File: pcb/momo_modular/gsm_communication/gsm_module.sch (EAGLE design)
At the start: 18 parts

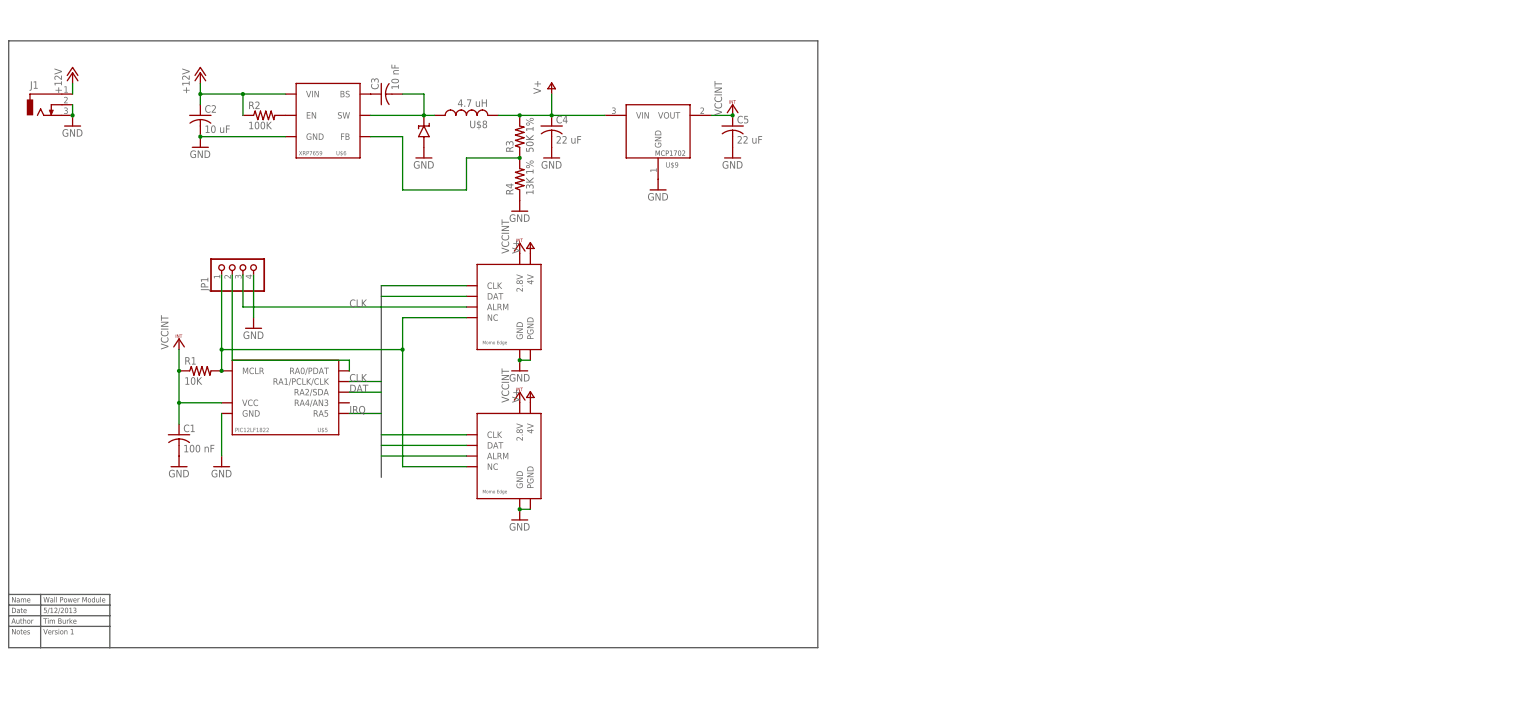
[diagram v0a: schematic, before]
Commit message: Laid out version 2 of the controller board and wall power board with better power supply layout to minimize noise coupling. Created version 1 of the gsm board. Changed Momo edge connector to an 8 pin version.
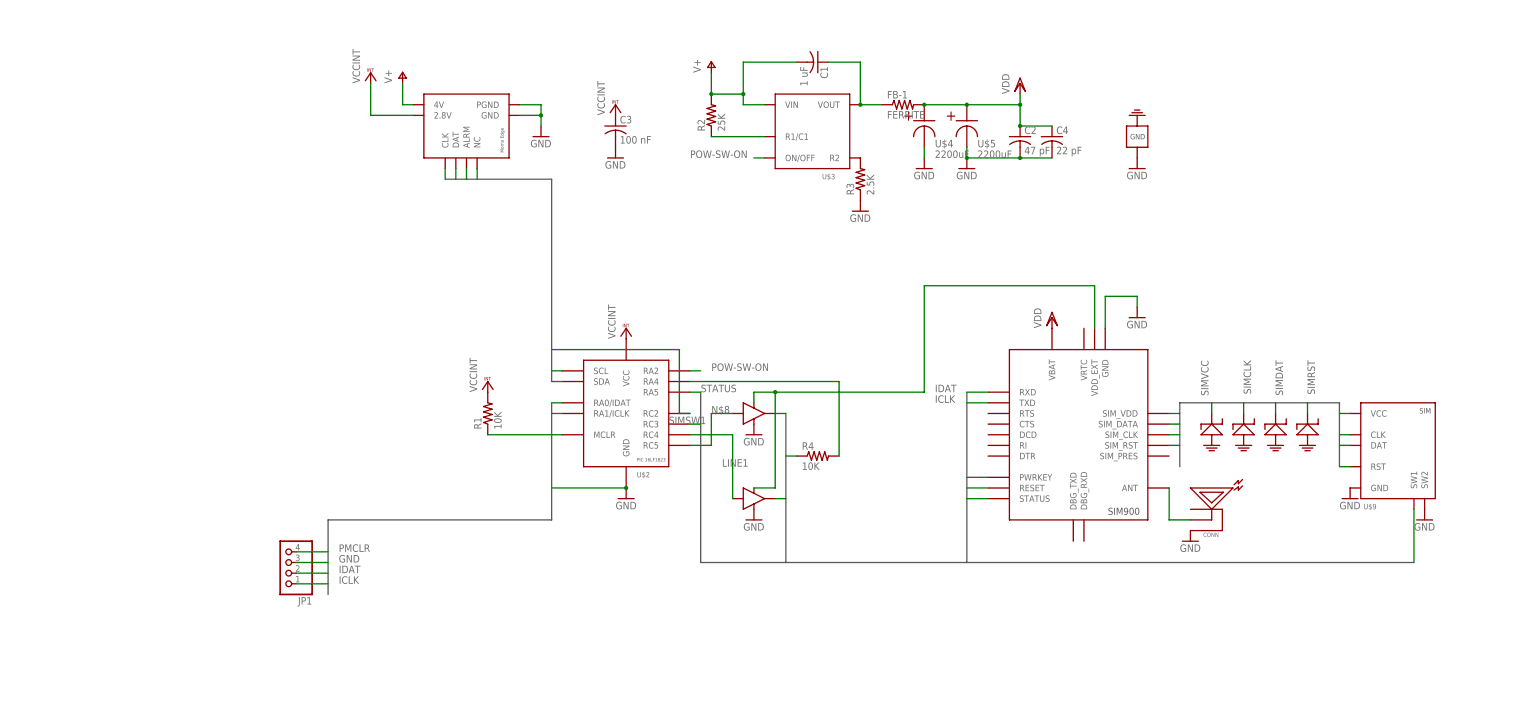
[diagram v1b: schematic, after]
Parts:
- removed C5: 22 uF, rcl:C-USC0402
- removed J1: (no value), con-jack:DCJ0303
- added CONN: RFANTENNA, components:RFANTENNA
- added FB-1: FERRITE, rcl:R-US_R0805
- added U$3: TI-HIGHSIDE-PFET, components:TI-HIGHSIDE-PFET
- added U$4: 2200uF, components:CAP-2200UF
- added U10: ESD-SMF05C, components:ESD-SMF05C
- C1: value 100 nF -> 1 uF; device rcl:C-USC0402 -> rcl:C-USC0402K
- C2: value 10 uF -> 47 pF; device rcl:C-USC0805 -> rcl:C-USC0402K
- C3: value 10 nF -> 100 nF
- C4: value 22 uF -> 22 pF; device rcl:C-USC1206 -> rcl:C-USC0402K
- R2: value 100K -> 25K
- R3: value 50K 1% -> 2.5K
- R4: value 13K 1% -> 10K
- U$1: value MOMO-EDGE-8F -> MOMO-EDGE-8M; device components:MOMO-EDGE-8F -> components:MOMO-EDGE-8M
- U$2: value MOMO-EDGE-8M -> PIC16LF1823; device components:MOMO-EDGE-8M -> components:PIC16LF1823
- U$5: value PIC12LF1822 -> 2200uF; device components:PIC12LF1822 -> components:CAP-2200UF
- U$6: value XRP7659 -> SIM900; device components:XRP7659 -> components:SIM900
- U$7: value DIODE_SS2P3 -> BUFFER-OD; device components:DIODE_SS2P3 -> components:BUFFER-OD
- U$8: value 4.7 uH -> BUFFER-OD; device components:NR6028-INDUCTOR -> components:BUFFER-OD
- U$9: value MCP1702 -> SIMHOLDER-8PIN; device components:MCP1702 -> components:SIMHOLDER-8PIN
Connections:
- removed net +12V: C2.1, J1.1, R2.1, U$6.VIN
- removed net CLK: JP1.3, U$1.CLK, U$2.CLK, U$5.RA1/PCLK/CLK
- removed net IRQ: U$1.ALRM, U$2.ALRM, U$5.RA5
- new net ALARM: U$1.ALRM, U$2.RC2
- new net CLOCK: U$1.CLK, U$2.SCL
- new net ICLK: JP1.1, U$2.RA1/ICLK, U$6.TXD
- new net IDAT: JP1.2, U$2.RA0/IDAT, U$6.RXD
- new net LINE1: U$2.RC4, U$8.IN
- new net N$7: CONN.PIN, U$6.ANT
- new net PMCLR: JP1.4, R1.1, U$1.NC, U$2.MCLR
- new net POW-SW-ON: U$2.RA2, U$3.ON/OFF
- new net PWRKEY: U$6.PWRKEY, U$7.OUT
- new net RESET: U$6.RESET, U$8.OUT
- new net SIMCLK: U$6.SIM_CLK, U$9.CLK, U10G$4.P$1
- new net SIMDAT: U$6.SIM_DATA, U$9.DAT, U10G$3.P$1
- new net SIMRST: U$6.SIM_RST, U$9.RST, U10G$2.P$1
- new net SIMSW1: R4.1, U$2.RC3, U$9.SW1
- new net SIMVCC: U$6.SIM_VDD, U$9.VCC, U10G$1.P$1
- new net STATUS: U$2.RA5, U$6.STATUS
- new net VDD: C2.1, C4.1, FB-1.2, U$4.+, U$5.+, U$6.VBAT
- net DAT: now also U$2.SDA; no longer U$2.DAT, U$5.RA2/SDA
- net GND: now also C3.2, CONN.SHIELD, JP1.3, R3.1, U$4.-, U$5.-, U$7.GND, U$8.GND, U$9.SW2, U10G$6.GND; no longer C1.2, C5.2, J1.2, J1.3, JP1.4, R4.1, U$2.PGND, U$5.GND, U$7.AN
- net N$1: now also R3.2, U$3.R2; no longer JP1.1, R1.2, U$1.NC, U$2.NC, U$5.MCLR
- net N$2: now also R4.2, U$2.RA4; no longer C3.2, U$6.SW, U$7.CATH, U$8.1
- net N$3: now also R2.1, U$3.R1/C1; no longer R2.2, U$6.EN
- net N$4: now also C1.1, FB-1.1, U$3.VOUT; no longer C3.1, U$6.BS
- net N$6: now also U$6.VDD_EXT, U$7.VCC, U$8.VCC; no longer R3.1, R4.2, U$6.FB
- net N$8: now also U$2.RC5, U$7.IN; no longer JP1.2, U$5.RA0/PDAT
- net V+: now also C1.2, R2.2, U$3.VIN; no longer C4.1, R3.2, U$2.4V, U$8.2, U$9.VIN
- net VCCINT: now also C3.1, R1.2, U$2.VCC; no longer C1.1, C5.1, R1.1, U$2.2.8V, U$5.VCC, U$9.VOUT
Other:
- note removed: "5/12/2013"
- note removed: "Author"
- note removed: "Date"
- note removed: "Name"
- note removed: "Notes"
- note removed: "Tim Burke"
- note removed: "Version 1"
- note removed: "Wall Power Module"
- moved on the sheet: C1, C2, C3, C4, JP1, R1, R2, R3, R4

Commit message: Finalized the following boards for fabrication/assembly: Sensor Dev Board GSM Module Combined Wallpower and Controller Boards
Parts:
- removed U$7, U$8: BUFFER-OD, components:BUFFER-OD
- added JP2: (no value), pinhead:PINHD-1X3
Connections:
- removed net LINE1: U$2.RC4, U$8.IN
- removed net N$6: U$6.VDD_EXT, U$7.VCC, U$8.VCC
- removed net N$8: U$2.RC5, U$7.IN
- new net DEBUGRX: JP2.2, U$6.DBG_RXD
- new net DEBUGTX: JP2.1, U$6.DBG_TXD
- net GND: now also JP2.3; no longer U$7.GND, U$8.GND
- net PWRKEY: now also U$2.RC5; no longer U$7.OUT
- net RESET: now also U$2.RC4; no longer U$8.OUT
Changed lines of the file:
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@@
 <part name="VDD2" library="supply1" deviceset="VDD" device=""/>
 <part name="GND7" library="supply1" deviceset="GND" device=""/>
-<part name="U$7" library="components" deviceset="BUFFER-OD" device=""/>
-<part name="U$8" library="components" deviceset="BUFFER-OD" device=""/>
-<part name="GND8" library="supply1" deviceset="GND" device=""/>
-<part name="GND9" library="supply1" deviceset="GND" device=""/>
 <part name="U$9" library="components" deviceset="SIMHOLDER-8PIN" device=""/>
 <part name="GND10" library="supply1" deviceset="GND" device=""/>
@@
 <part name="C4" library="rcl" deviceset="C-US" device="C0402K" value="22 pF"/>
 <part name="R4" library="rcl" deviceset="R-US_" device="R0603" value="10K"/>
+<part name="JP2" library="pinhead" deviceset="PINHD-1X3" device=""/>
+<part name="GND6" library="supply1" deviceset="GND" device=""/>
 </parts>
 <sheets>
@@
 <instance part="VDD2" gate="G$1" x="152.4" y="40.64"/>
 <instance part="GND7" gate="1" x="172.72" y="40.64"/>
-<instance part="U$7" gate="G$1" x="81.28" y="17.78"/>
-<instance part="U$8" gate="G$1" x="81.28" y="-2.54"/>
-<instance part="GND8" gate="1" x="81.28" y="12.7"/>
-<instance part="GND9" gate="1" x="81.28" y="-7.62"/>
 <instance part="U$9" gate="G$1" x="226.06" y="5.08"/>
 <instance part="GND10" gate="1" x="241.3" y="-7.62"/>
@@
 <instance part="C4" gate="G$1" x="152.4" y="83.82"/>
 <instance part="R4" gate="G$1" x="96.52" y="7.62"/>
+<instance part="JP2" gate="A" x="170.18" y="-30.48"/>
+<instance part="GND6" gate="1" x="160.02" y="-40.64"/>
 </instances>
 <busses>
@@
 </segment>
 <segment>
-<pinref part="U$7" gate="G$1" pin="GND"/>
-<pinref part="GND8" gate="1" pin="GND"/>
-</segment>
-<segment>
-<pinref part="U$8" gate="G$1" pin="GND"/>
-<pinref part="GND9" gate="1" pin="GND"/>
-</segment>
-<segment>
 <pinref part="U$9" gate="G$1" pin="SW2"/>
 <pinref part="GND10" gate="1" pin="GND"/>
@@
 <pinref part="GND12" gate="1" pin="GND"/>
 <pinref part="U10" gate="G$6" pin="GND"/>
+</segment>
+<segment>
+<pinref part="GND6" gate="1" pin="GND"/>
+<wire x1="160.02" y1="-38.1" x2="160.02" y2="-33.02" width="0.1524" layer="91"/>
+<pinref part="JP2" gate="A" pin="3"/>
+<wire x1="160.02" y1="-33.02" x2="167.64" y2="-33.02" width="0.1524" layer="91"/>
 </segment>
 </net>
@@
 <net name="PWRKEY" class="0">
 <segment>
-<pinref part="U$7" gate="G$1" pin="OUT"/>
-<wire x1="86.36" y1="17.78" x2="88.9" y2="17.78" width="0.1524" layer="91"/>
+<pinref part="U$2" gate="G$1" pin="RC5"/>
+<wire x1="66.04" y1="10.16" x2="71.12" y2="10.16" width="0.1524" layer="91"/>
+<wire x1="71.12" y1="10.16" x2="71.12" y2="17.78" width="0.1524" layer="91"/>
+<label x="71.12" y="17.78" size="1.778" layer="95"/>
+<wire x1="71.12" y1="17.78" x2="88.9" y2="17.78" width="0.1524" layer="91"/>
 </segment>
 <segment>
@@
 <net name="RESET" class="0">
 <segment>
-<pinref part="U$8" gate="G$1" pin="OUT"/>
-<wire x1="86.36" y1="-2.54" x2="88.9" y2="-2.54" width="0.1524" layer="91"/>
+<pinref part="U$2" gate="G$1" pin="RC4"/>
+<wire x1="66.04" y1="12.7" x2="76.2" y2="12.7" width="0.1524" layer="91"/>
+<wire x1="76.2" y1="12.7" x2="76.2" y2="-2.54" width="0.1524" layer="91"/>
+<wire x1="76.2" y1="-2.54" x2="88.9" y2="-2.54" width="0.1524" layer="91"/>
 </segment>
 <segment>
@@
 </segment>
 </net>
-<net name="N$8" class="0">
-<segment>
-<pinref part="U$2" gate="G$1" pin="RC5"/>
-<wire x1="66.04" y1="10.16" x2="71.12" y2="10.16" width="0.1524" layer="91"/>
-<wire x1="71.12" y1="10.16" x2="71.12" y2="17.78" width="0.1524" layer="91"/>
-<pinref part="U$7" gate="G$1" pin="IN"/>
-<wire x1="71.12" y1="17.78" x2="76.2" y2="17.78" width="0.1524" layer="91"/>
-<label x="71.12" y="17.78" size="1.778" layer="95"/>
-</segment>
-</net>
-<net name="N$6" class="0">
-<segment>
-<pinref part="U$8" gate="G$1" pin="VCC"/>
-<wire x1="81.28" y1="0" x2="86.36" y2="0" width="0.1524" layer="91"/>
-<wire x1="86.36" y1="0" x2="86.36" y2="22.86" width="0.1524" layer="91"/>
-<pinref part="U$7" gate="G$1" pin="VCC"/>
-<wire x1="86.36" y1="22.86" x2="81.28" y2="22.86" width="0.1524" layer="91"/>
-<wire x1="81.28" y1="22.86" x2="81.28" y2="20.32" width="0.1524" layer="91"/>
-<wire x1="86.36" y1="22.86" x2="121.92" y2="22.86" width="0.1524" layer="91"/>
-<wire x1="121.92" y1="22.86" x2="121.92" y2="48.26" width="0.1524" layer="91"/>
-<junction x="86.36" y="22.86"/>
-<pinref part="U$6" gate="G$1" pin="VDD_EXT"/>
-<wire x1="121.92" y1="48.26" x2="162.56" y2="48.26" width="0.1524" layer="91"/>
-<wire x1="162.56" y1="48.26" x2="162.56" y2="38.1" width="0.1524" layer="91"/>
-</segment>
-</net>
-<net name="LINE1" class="0">
-<segment>
-<pinref part="U$2" gate="G$1" pin="RC4"/>
-<wire x1="66.04" y1="12.7" x2="76.2" y2="12.7" width="0.1524" layer="91"/>
-<label x="73.66" y="5.08" size="1.778" layer="95"/>
-<pinref part="U$8" gate="G$1" pin="IN"/>
-<wire x1="76.2" y1="12.7" x2="76.2" y2="-2.54" width="0.1524" layer="91"/>
-</segment>
-</net>
 <net name="N$2" class="0">
 <segment>
@@
 </segment>
 </net>
+<net name="DEBUGRX" class="0">
+<segment>
+<pinref part="U$6" gate="G$1" pin="DBG_RXD"/>
+<wire x1="160.02" y1="-12.7" x2="160.02" y2="-30.48" width="0.1524" layer="91"/>
+<pinref part="JP2" gate="A" pin="2"/>
+<wire x1="160.02" y1="-30.48" x2="167.64" y2="-30.48" width="0.1524" layer="91"/>
+</segment>
+</net>
+<net name="DEBUGTX" class="0">
+<segment>
+<pinref part="U$6" gate="G$1" pin="DBG_TXD"/>
+<pinref part="JP2" gate="A" pin="1"/>
+<wire x1="157.48" y1="-27.94" x2="157.48" y2="-12.7" width="0.1524" layer="91"/>
+<wire x1="157.48" y1="-27.94" x2="167.64" y2="-27.94" width="0.1524" layer="91"/>
+</segment>
+</net>

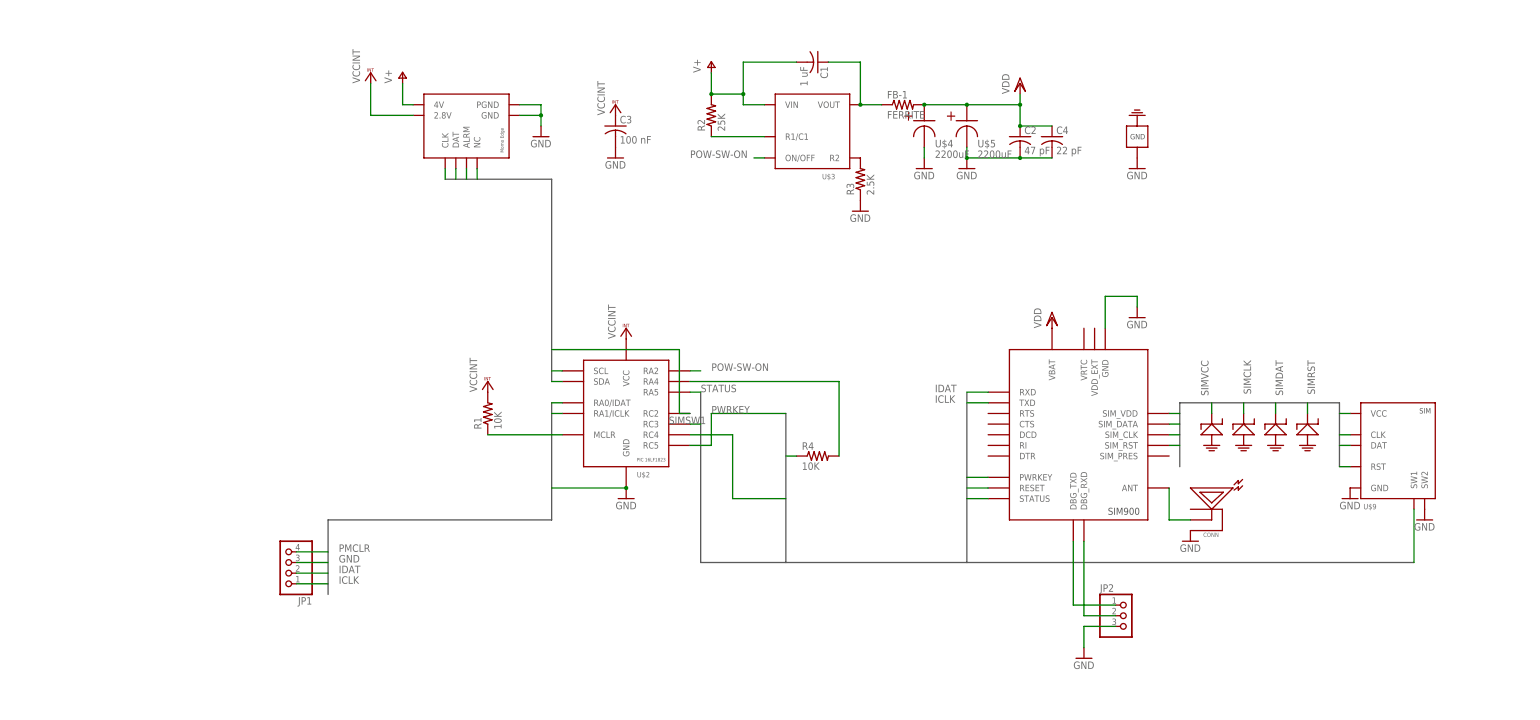
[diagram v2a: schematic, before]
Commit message: Finished next version of hardware.  Working on automatic BOM generation for purchasing.
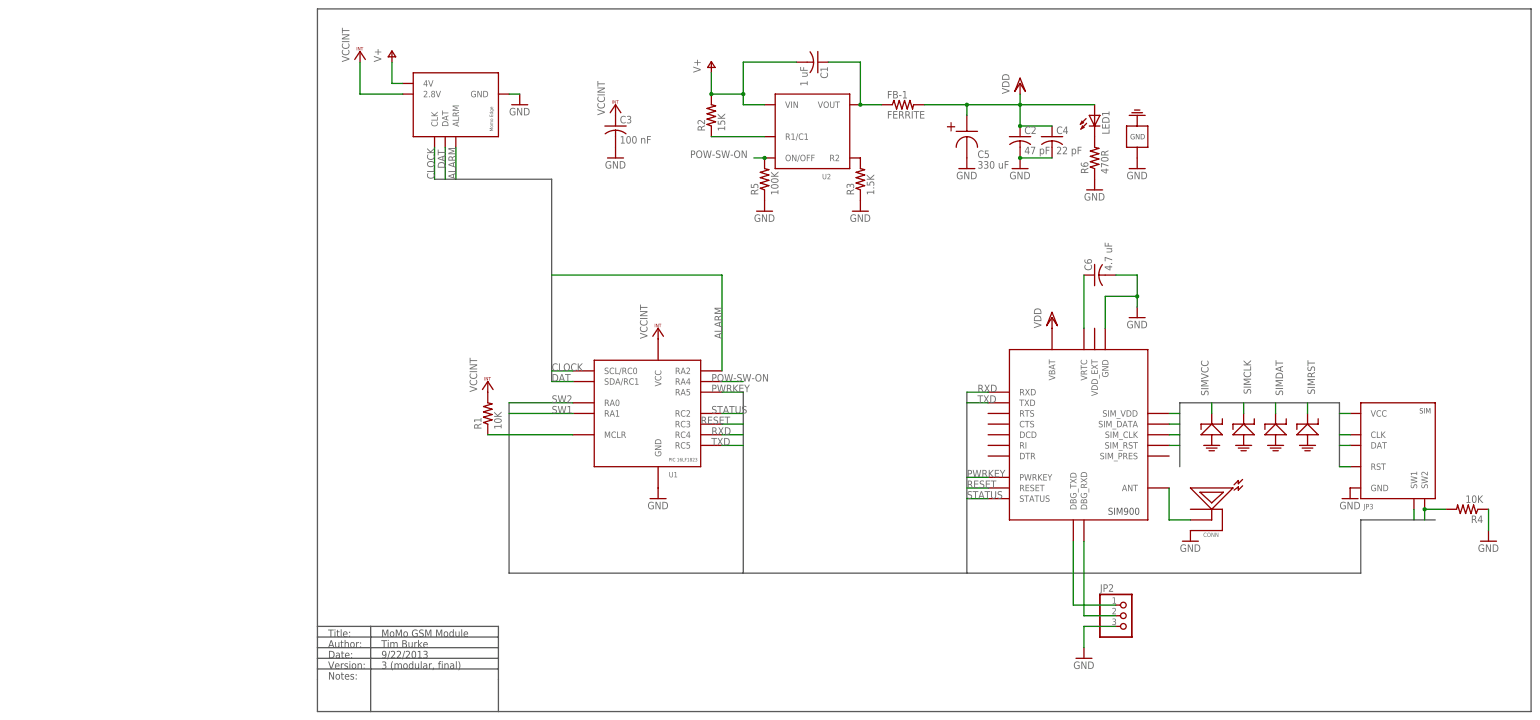
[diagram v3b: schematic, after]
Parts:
- removed U$1: MOMO-EDGE-8M, components:MOMO-EDGE-8M
- removed U$2: PIC16LF1823, components:PIC16LF1823
- removed U$4, U$5: 2200uF, components:CAP-2200UF
- removed U$9: SIMHOLDER-8PIN, components:SIMHOLDER-8PIN
- added C5: 330 uF, components:TANTALUM_CAP
- added C6: 4.7 uF, rcl:C-USC0805
- added JP3: SIMHOLDER-8PINHING, components:SIMHOLDER-8PINHING
- added LED1: (no value), led:LEDCHIPLED_0603
- added R5: 100K, rcl:R-US_R0603
- added R6: 470R, rcl:R-US_R0603
- added U1: PIC16LF1823, components:PIC16LF1823
- C1: DIGIKEY-PN (none) -> 445-4114-1-ND
- C2: DIGIKEY-PN (none) -> 445-1243-1-ND
- C3: DIGIKEY-PN (none) -> 445-1265-1-ND
- C4: DIGIKEY-PN (none) -> 445-1239-1-ND
- CONN: DIGIKEY-PN (none) -> J983CT-ND
- FB-1: DIGIKEY-PN (none) -> 445-1567-1-ND
- JP1: value (none) -> MOMO-EDGE-6M; device pinhead:PINHD-1X4 -> components:MOMO-EDGE-6M
- R1, R4: DIGIKEY-PN (none) -> P10.0KHCT-ND
- R2: value 25K -> 15K; DIGIKEY-PN (none) -> P15KGCT-ND
- R3: value 2.5K -> 1.5K; DIGIKEY-PN (none) -> P1.5KGCT-ND
- renumbered U$3 to U2, U$6 to U3, U10 to U4
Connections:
- removed net ICLK: JP1.1, U$2.RA1/ICLK, U3.TXD
- removed net IDAT: JP1.2, U$2.RA0/IDAT, U3.RXD
- removed net PMCLR: JP1.4, R1.1, U$1.NC, U$2.MCLR
- removed net SIMSW1: R4.1, U$2.RC3, U$9.SW1
- new net N$5: C6.1, U3.VRTC
- new net N$6: R1.1, U1.MCLR
- new net RXD: U1.RC4, U3.RXD
- new net SW1: JP3.SW1, U1.RA1
- new net SW2: JP3.SW2, R4.2, U1.RA0
- new net TXD: U1.RC5, U3.TXD
- net ALARM: now also JP1.ALRM, U1.RA2; no longer U$1.ALRM, U$2.RC2
- net CLOCK: now also JP1.CLK, U1.SCL/RC0; no longer U$1.CLK, U$2.SCL
- net DAT: now also JP1.DAT, U1.SDA/RC1; no longer U$1.DAT, U$2.SDA
- net GND: now also C5.-, C6.2, JP1.GND, JP3.GND, R4.1, R5.1, R6.1, U1.GND; no longer JP1.3, U$1.GND, U$1.PGND, U$2.GND, U$4.-, U$5.-, U$9.GND, U$9.SW2
- net N$2: now also LED1.C, R6.2; no longer R4.2, U$2.RA4
- net POW-SW-ON: now also R5.2, U1.RA4; no longer U$2.RA2
- net PWRKEY: now also U1.RA5; no longer U$2.RC5
- net RESET: now also U1.RC3; no longer U$2.RC4
- net SIMCLK: now also JP3.CLK; no longer U$9.CLK
- net SIMDAT: now also JP3.DAT; no longer U$9.DAT
- net SIMRST: now also JP3.RST; no longer U$9.RST
- net SIMVCC: now also JP3.VCC; no longer U$9.VCC
- net STATUS: now also U1.RC2; no longer U$2.RA5
- net V+: now also JP1.4V; no longer U$1.4V
- net VCCINT: now also JP1.2.8V, U1.VCC; no longer U$1.2.8V, U$2.VCC
- net VDD: now also C5.+, LED1.A; no longer U$4.+, U$5.+
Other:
- note added: "3 (modular, final)"
- note added: "9/22/2013"
- note added: "Author:"
- note added: "Date:"
- note added: "MoMo GSM Module"
- note added: "Notes:"
- note added: "Tim Burke"
- note added: "Title:"
- note added: "Version:"
- moved on the sheet: R4
